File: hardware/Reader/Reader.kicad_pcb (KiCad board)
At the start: 4 copper layers, 136 parts, among them CN1 AHDF15A-KG-TAXB

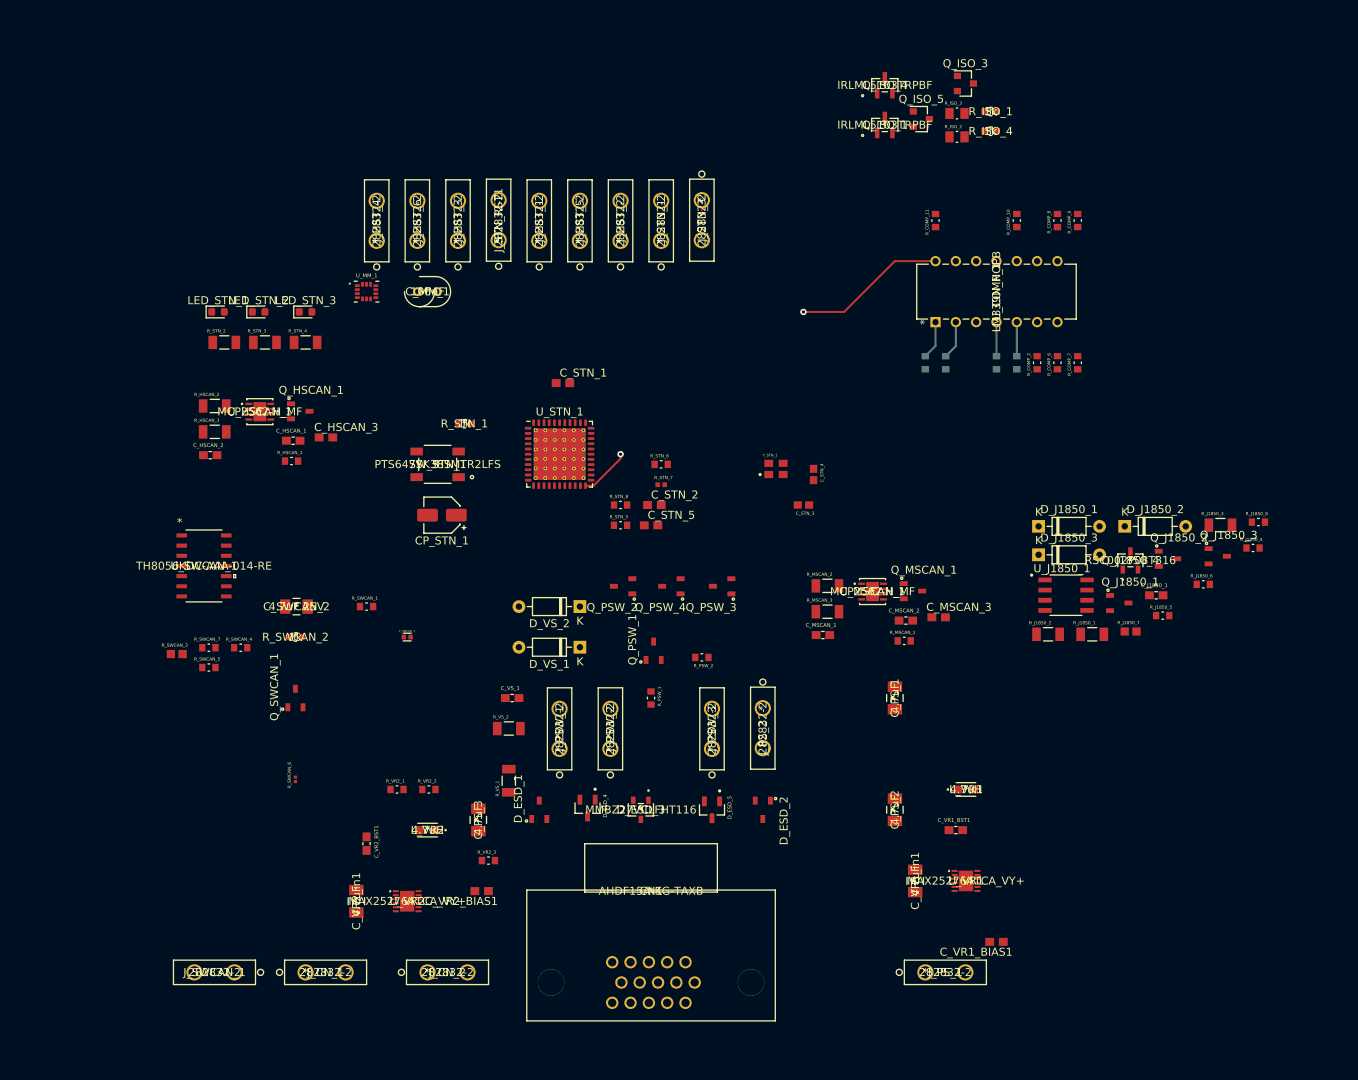
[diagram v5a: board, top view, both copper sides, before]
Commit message: Fixed wiring issue on ESD Protection
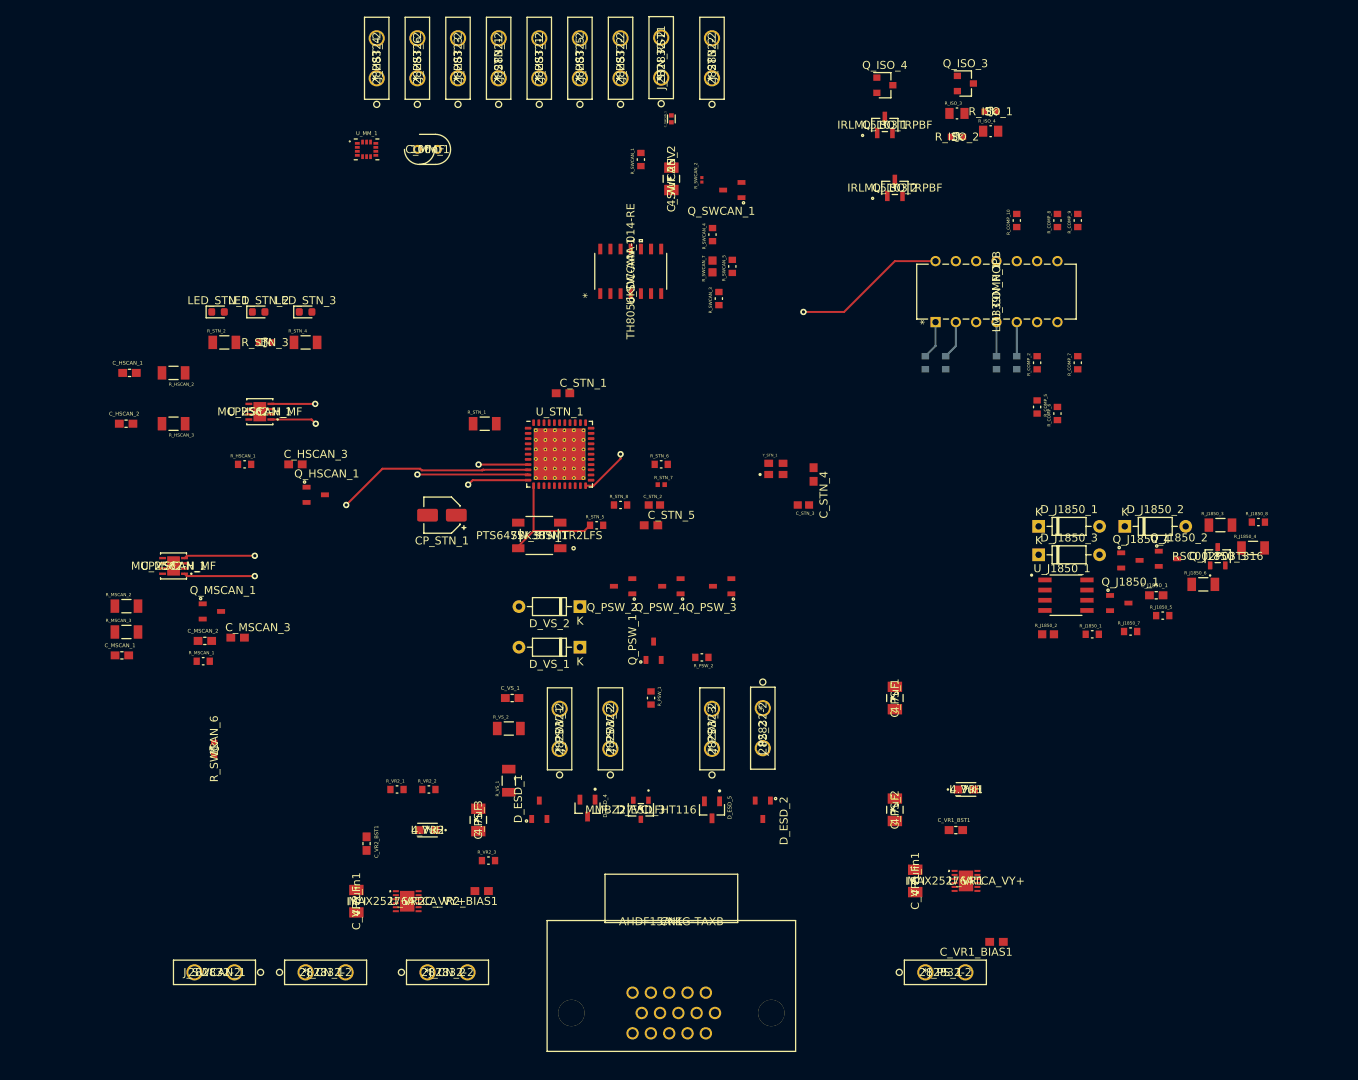
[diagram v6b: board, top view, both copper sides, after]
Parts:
- removed J_STN_3: 282832-2, footprints:282832-2
- removed Q_ISO_5: MMBT3904WT1G, Package_TO_SOT_SMD:SOT-23
- removed R_COMP5, R_COMP_11: 10k, footprints:RESC1608X55N
- added J_STN_2: 282832-2, footprints:282832-2, F.Cu at (147.3, 35.6)
- added Q_ISO_2: IRLML5103TRPBF, footprints:IRLML5103TRPBF, F.Cu at (170.2, 49.3)
- added R_COMP1: 10k, footprints:RESC1608X55N, B.Cu at (174.0, 71.1)
- added R_COMP_5: 10k, footprints:RESC1608X55N, F.Cu at (188.0, 76.7)
- C_STN_2: value 1uF -> 30pF; footprint footprints:0603 -> footprints:CAPC1608X90N
- C_STN_4: value 30pF -> 1uF; footprint footprints:CAPC1608X90N -> footprints:0603
- D_ESD_4, D_ESD_5: footprint footprints:SOT95P237X111-3N -> SOT95P237X111-3N
- Q_ISO_4: value IRLML5103TRPBF -> MMBT3904WT1G; footprint footprints:IRLML5103TRPBF -> Package_TO_SOT_SMD:SOT-23
- Q_J1850_3: value NX7002AK,215 -> RSC002P03T316; footprint footprints:SOT95P230X110-3N -> footprints:RSC002P03T316
- Q_J1850_4: value RSC002P03T316 -> NX7002AK,215; footprint footprints:RSC002P03T316 -> footprints:SOT95P230X110-3N
- R_COMP_7: value 10k -> 2.7k
- R_COMP_8: value 2.7k -> 10k
- R_ISO_2: value 510k/0.5W -> 1k; footprint footprints:RESC2012X70N -> footprints:RC1608F102CS
- R_ISO_4: value 1k -> 510k/0.5W; footprint footprints:RC1608F102CS -> footprints:RESC2012X70N
- R_J1850_1: value 374 -> 10k; footprint footprints:RESC3216X70N -> footprints:RESC1608X55N
- R_J1850_2: value 866 -> 1.5k; footprint footprints:RESC3216X70N -> footprints:RESC1607X60N
- R_J1850_3: value 240 -> 866
- R_J1850_4: value 10k -> 374; footprint footprints:RESC1608X55N -> footprints:RESC3216X70N
- R_J1850_6: value 10k -> 240; footprint footprints:RESC1608X55N -> footprints:RESC3216X70N
- R_J1850_7: value 1.5k -> 10k; footprint footprints:RESC1607X60N -> footprints:RESC1608X55N
- R_STN_1: value 1k -> 330; footprint footprints:RC1608F102CS -> footprints:RESC3216X70N
- R_STN_3: value 330 -> 1k; footprint footprints:RESC3216X70N -> footprints:RC1608F102CS
- R_SWCAN_1: value 6.49k 0.12W -> 10k
- R_SWCAN_2: value 1k -> 130; footprint footprints:RC1608F102CS -> footprints:RESC0603X26N
- R_SWCAN_3: value 1.5k -> 6.49k 0.12W; footprint footprints:RESC1607X60N -> footprints:RESC1608X55N
- R_SWCAN_6: value 130 -> 1k; footprint footprints:RESC0603X26N -> footprints:RC1608F102CS
- R_SWCAN_7: value 10k -> 1.5k; footprint footprints:RESC1608X55N -> footprints:RESC1607X60N
- moved C_MSCAN_2 87.7 mm to (83.9, 105.9)
- moved C_MSCAN_3 87.7 mm to (88.0, 105.5)
- moved R_MSCAN_2 87.7 mm to (74.1, 101.5)
- moved R_MSCAN_3 87.7 mm to (74.1, 104.8)
- moved C_MSCAN_1 87.7 mm to (73.6, 107.7)
- moved Q_MSCAN_1 87.7 mm to (84.8, 102.2)
- moved R_MSCAN_1 87.7 mm to (83.7, 108.4)
- moved U_MSCAN_1 87.4 mm to (80.0, 96.5), turned to 180 degrees
- moved Q_SWCAN_1 83.8 mm to (149.9, 49.5), turned to 180 degrees
- moved R_SWCAN_5 82.4 mm to (149.9, 59.1), turned to 90 degrees
- moved R_SWCAN_3 81.0 mm to (148.2, 63.1), turned to 90 degrees
- moved R_SWCAN_7 79.0 mm to (147.4, 59.1), turned to 90 degrees
- moved R_SWCAN_4 78.4 mm to (147.4, 55.1), turned to 90 degrees
- moved R_SWCAN_2 76.5 mm to (146.1, 48.3), turned to 90 degrees
- moved C_SWCAN_1 72.7 mm to (142.2, 40.6), turned to 90 degrees
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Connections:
- CN1 pad 11: Pin14_ISO15765-4_CAN_BUS_Low -> Pin6_ISO15765_CAN_BUS_High
- CN1 pad 12: Pin14_ISO15765-4_CAN_BUS_Low -> Pin14_ISO15765_CAN_BUS_Low
- CN1 pad 6: Pin15_ISO9141_L-Line -> Pin7_ISO9141_K-Line
- C_STN_2 pad 1: +3V3 -> Pin4_GnD_Chassis
- C_STN_2 pad 2: Pin4_GnD_Chassis -> Net-(C_STN_2-Pad2)
- C_STN_3 pad 1: Pin4_GnD_Chassis -> Net-(C_STN_3-Pad1)
- C_STN_3 pad 2: Net-(C_STN_3-Pad2) -> Pin4_GnD_Chassis
- C_STN_5 pad 1: Net-(C_STN_5-Pad1) -> +3V3
- D_ESD_1 pad 1: Pin14_ISO15765-4_CAN_BUS_Low -> Pin6_ISO15765_CAN_BUS_High
- D_ESD_1 pad 2: Pin14_ISO15765-4_CAN_BUS_Low -> Pin14_ISO15765_CAN_BUS_Low
- D_ESD_4 pad 1: Pin15_ISO9141_L-Line -> Pin7_ISO9141_K-Line
- D_J1850_1 pad 1: Net-(D_J1850_1-Pad1) -> Pin2_SAE_J1850_BUS+
- D_J1850_1 pad 2: +5V_SW -> Net-(D_J1850_1-Pad2)
- D_J1850_2 pad 1: Pin2_SAE_J1850_BUS+ -> Pin4_GnD_Chassis
- D_J1850_3 pad 1: Pin4_GnD_Chassis -> Net-(D_J1850_3-Pad1)
- D_J1850_3 pad 2: Net-(D_J1850_3-Pad2) -> +5V_SW
- J_CN_1 pad 1: Pin14_ISO15765-4_CAN_BUS_Low -> Pin6_ISO15765_CAN_BUS_High
- J_CN_1 pad 2: Pin14_ISO15765-4_CAN_BUS_Low -> Pin14_ISO15765_CAN_BUS_Low
- J_CN_2 pad 1: Pin15_ISO9141_L-Line -> Pin7_ISO9141_K-Line
- J_HST_2 pad 1: /Host/HOST_RX -> +5V
- J_HST_2 pad 2: /Host/HOST_TX -> Pin4_GnD_Chassis
- J_HST_3 pad 1: /Host/I2C_SCL -> /Host/HOST_RX
- J_HST_3 pad 2: /Host/I2C_SDA -> /Host/HOST_TX
- J_HST_4 pad 1: /Host/MEMS_INT -> /Host/I2C_SCL
- J_HST_4 pad 2: /Host/MEMS_CS -> /Host/I2C_SDA
- J_HST_5 pad 1: +5V -> Pin4_GnD_Chassis
- J_HST_5 pad 2: Pin4_GnD_Chassis -> /Host/MEMS_CS
- J_HST_6 pad 1: Pin4_GnD_Chassis -> /Host/MEMS_INT
- Q_ISO_3 pad 3: Pin15_ISO9141_L-Line -> Pin7_ISO9141_K-Line
- Q_ISO_4 pad 1: /OBDII Interpreter/PWR_CTRL -> Net-(Q_ISO_4-Pad1)
- Q_ISO_4 pad 2: Net-(Q_ISO_4-Pad2) -> Pin4_GnD_Chassis
- Q_ISO_4 pad 3: +12V -> Pin15_ISO9141_L-Line
- Q_J1850_2 pad 1: /OBDII Interpreter/OBDII Chip/J1850_BUS-_TX -> /OBDII Interpreter/OBDII Chip/J1850_BUS+_TX
- Q_J1850_2 pad 3: Pin10_SAE_J1850_BUS- -> Net-(Q_J1850_2-Pad3)
- Q_J1850_3 pad 1: /OBDII Interpreter/OBDII Chip/J1850_BUS+_TX -> Net-(Q_J1850_2-Pad3)
- Q_J1850_3 pad 2: Pin4_GnD_Chassis -> +V_J1850
- Q_J1850_3 pad 3: Net-(Q_J1850_3-Pad3) -> Net-(D_J1850_1-Pad2)
- Q_J1850_4 pad 1: Net-(Q_J1850_3-Pad3) -> /OBDII Interpreter/OBDII Chip/J1850_BUS-_TX
- Q_J1850_4 pad 2: +V_J1850 -> Pin4_GnD_Chassis
- Q_J1850_4 pad 3: Net-(D_J1850_2-Pad2) -> Pin10_SAE_J1850_BUS-
- R_COMP_10 pad 1: Net-(R_COMP_10-Pad1) -> +3V3
- R_COMP_10 pad 2: Pin2_SAE_J1850_BUS+ -> /OBDII Interpreter/Comparator Transceiver/VPW_RX
- R_COMP_2 pad 1: Pin15_ISO9141_L-Line -> Pin7_ISO9141_K-Line
- R_COMP_6 pad 1: +12V_SW -> Net-(R_COMP_5-Pad2)
- R_COMP_6 pad 2: Net-(R_COMP_6-Pad2) -> Pin4_GnD_Chassis
- R_COMP_7 pad 1: Net-(R_COMP_6-Pad2) -> +5V_SW
- R_COMP_7 pad 2: Pin4_GnD_Chassis -> Net-(R_COMP_7-Pad2)
- R_COMP_8 pad 1: +5V_SW -> Net-(R_COMP_7-Pad2)
- R_COMP_8 pad 2: Net-(R_COMP_8-Pad2) -> Pin4_GnD_Chassis
- R_COMP_9 pad 1: Net-(R_COMP_8-Pad2) -> Net-(R_COMP_9-Pad1)
- R_COMP_9 pad 2: Pin4_GnD_Chassis -> Pin2_SAE_J1850_BUS+
- R_HSCAN_2 pad 1: Pin14_ISO15765-4_CAN_BUS_Low -> Pin14_ISO15765_CAN_BUS_Low
- R_HSCAN_3 pad 1: Pin14_ISO15765-4_CAN_BUS_Low -> Pin6_ISO15765_CAN_BUS_High
- R_ISO_2 pad 1: Pin15_ISO9141_L-Line -> Net-(Q_ISO_4-Pad1)
- R_ISO_2 pad 2: Net-(Q_ISO_1-Pad2) -> /OBDII Interpreter/ISO 9141/ISO 14230 Transceiver/~ISO_L_TX~
- R_ISO_3 pad 1: Pin15_ISO9141_L-Line -> Pin7_ISO9141_K-Line
- R_ISO_3 pad 2: Net-(Q_ISO_4-Pad2) -> Net-(Q_ISO_1-Pad2)
- R_ISO_4 pad 1: Net-(Q_ISO_5-Pad1) -> Pin15_ISO9141_L-Line
- R_ISO_4 pad 2: /OBDII Interpreter/ISO 9141/ISO 14230 Transceiver/~ISO_L_TX~ -> Net-(Q_ISO_2-Pad2)
- R_J1850_1 pad 1: Net-(Q_J1850_1-Pad3) -> /OBDII Interpreter/OBDII Chip/J1850_BUS+_TX
- R_J1850_2 pad 1: Net-(Q_J1850_1-Pad3) -> +V_J1850
- R_J1850_2 pad 2: Net-(R_J1850_2-Pad2) -> Net-(Q_J1850_2-Pad3)
- R_J1850_3 pad 1: +V_J1850 -> Net-(Q_J1850_1-Pad3)
- R_J1850_3 pad 2: Net-(R_J1850_2-Pad2) -> Net-(R_J1850_3-Pad2)
- R_J1850_4 pad 1: /OBDII Interpreter/OBDII Chip/J1850_BUS-_TX -> Net-(Q_J1850_1-Pad3)
- R_J1850_5 pad 1: Net-(D_J1850_1-Pad1) -> Pin2_SAE_J1850_BUS+
- R_J1850_5 pad 2: Pin10_SAE_J1850_BUS- -> Net-(D_J1850_2-Pad2)
- R_J1850_6 pad 1: /OBDII Interpreter/OBDII Chip/J1850_BUS+_TX -> +V_J1850
- R_J1850_6 pad 2: Pin4_GnD_Chassis -> Net-(R_J1850_3-Pad2)
- R_J1850_7 pad 1: +V_J1850 -> /OBDII Interpreter/OBDII Chip/J1850_BUS-_TX
- R_J1850_7 pad 2: Net-(Q_J1850_3-Pad3) -> Pin4_GnD_Chassis
- R_J1850_8 pad 1: Pin2_SAE_J1850_BUS+ -> Net-(D_J1850_3-Pad1)
- R_J1850_8 pad 2: Net-(D_J1850_3-Pad2) -> Pin10_SAE_J1850_BUS-
- R_STN_1 pad 1: +3V3 -> Net-(LED_STN_1-Pad1)
- R_STN_1 pad 2: /Host/HOST_TX -> /OBDII Interpreter/OBDII Chip/STATUS_LED
- R_STN_2 pad 1: Net-(LED_STN_1-Pad1) -> Net-(LED_STN_2-Pad1)
- R_STN_2 pad 2: /OBDII Interpreter/OBDII Chip/STATUS_LED -> /OBDII Interpreter/~RESET_OBD_HW~
- R_STN_3 pad 1: Net-(LED_STN_2-Pad1) -> +3V3
- R_STN_3 pad 2: /OBDII Interpreter/~RESET_OBD_HW~ -> /Host/HOST_TX
- R_SWCAN_1 pad 1: Pin1_SW_CAN -> /OBDII Interpreter/OBDII Chip/SW_CAN_LOAD
- R_SWCAN_1 pad 2: Net-(R_SWCAN_1-Pad2) -> Pin4_GnD_Chassis
- R_SWCAN_2 pad 1: /OBDII Interpreter/OBDII Chip/SW_CAN_RX -> Net-(J_SWCAN_1-Pad2)
- R_SWCAN_2 pad 2: +3V3 -> Net-(Q_SWCAN_1-Pad3)
- R_SWCAN_3 pad 1: /OBDII Interpreter/OBDII Chip/SW_CAN_TX -> Pin1_SW_CAN
- R_SWCAN_3 pad 2: +5V -> Net-(R_SWCAN_3-Pad2)
- R_SWCAN_6 pad 1: Net-(J_SWCAN_1-Pad2) -> /OBDII Interpreter/OBDII Chip/SW_CAN_RX
- R_SWCAN_6 pad 2: Net-(Q_SWCAN_1-Pad3) -> +3V3
- R_SWCAN_7 pad 1: /OBDII Interpreter/OBDII Chip/SW_CAN_LOAD -> /OBDII Interpreter/OBDII Chip/SW_CAN_TX
- R_SWCAN_7 pad 2: Pin4_GnD_Chassis -> +5V
- U_COMP_1 pad 7: Net-(R_COMP_6-Pad2) -> Net-(R_COMP_5-Pad2)
- U_COMP_1 pad 8: Net-(R_COMP_8-Pad2) -> Net-(R_COMP_7-Pad2)
- U_COMP_1 pad 9: Net-(R_COMP_10-Pad1) -> Net-(R_COMP_9-Pad1)
- U_HSCAN_1 pad 6: Pin14_ISO15765-4_CAN_BUS_Low -> Pin14_ISO15765_CAN_BUS_Low
- U_HSCAN_1 pad 7: Pin14_ISO15765-4_CAN_BUS_Low -> Pin6_ISO15765_CAN_BUS_High
- U_J1850_1 pad 4: Net-(R_J1850_2-Pad2) -> Net-(R_J1850_3-Pad2)
- U_STN_1 pad 29: Net-(C_STN_5-Pad1) -> Net-(C_STN_4-Pad1)
- U_STN_1 pad 30: Net-(C_STN_4-Pad1) -> Net-(C_STN_3-Pad1)
- U_STN_1 pad 31: Net-(C_STN_3-Pad2) -> Net-(C_STN_2-Pad2)
- U_SWCAN_1 pad 11: Net-(R_SWCAN_1-Pad2) -> Net-(R_SWCAN_3-Pad2)
- Y_STN_1 pad 1: Net-(C_STN_3-Pad2) -> Net-(C_STN_2-Pad2)
- Y_STN_1 pad 3: Net-(C_STN_4-Pad1) -> Net-(C_STN_3-Pad1)
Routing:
- net /OBDII Interpreter/High Speed CAN Transceiver/HS_CAN_RX: track 0.00 -> 89.3 mm, vias 0 -> 2
- net /OBDII Interpreter/High Speed CAN Transceiver/HS_CAN_TX: track 0.00 -> 88.8 mm, vias 0 -> 2
- net /OBDII Interpreter/Medium Speed CAN Transceiver/MS_CAN_TX: track 0.00 -> 49.0 mm, vias 0 -> 2
- net /OBDII Interpreter/Medium Speed CAN Transceiver/MS_CAN_RX: track 0.00 -> 47.0 mm, vias 0 -> 2
- net /OBDII Interpreter/~RESET_OBD_HW~: track 0.11 -> 16.1 mm
- net /OBDII Interpreter/~PWR_CTRL~: track 1.27 -> 0.00 mm

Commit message: Fixed minor bugs in schematic. Completed PCB layout v0.0.1 and exported Gerber files
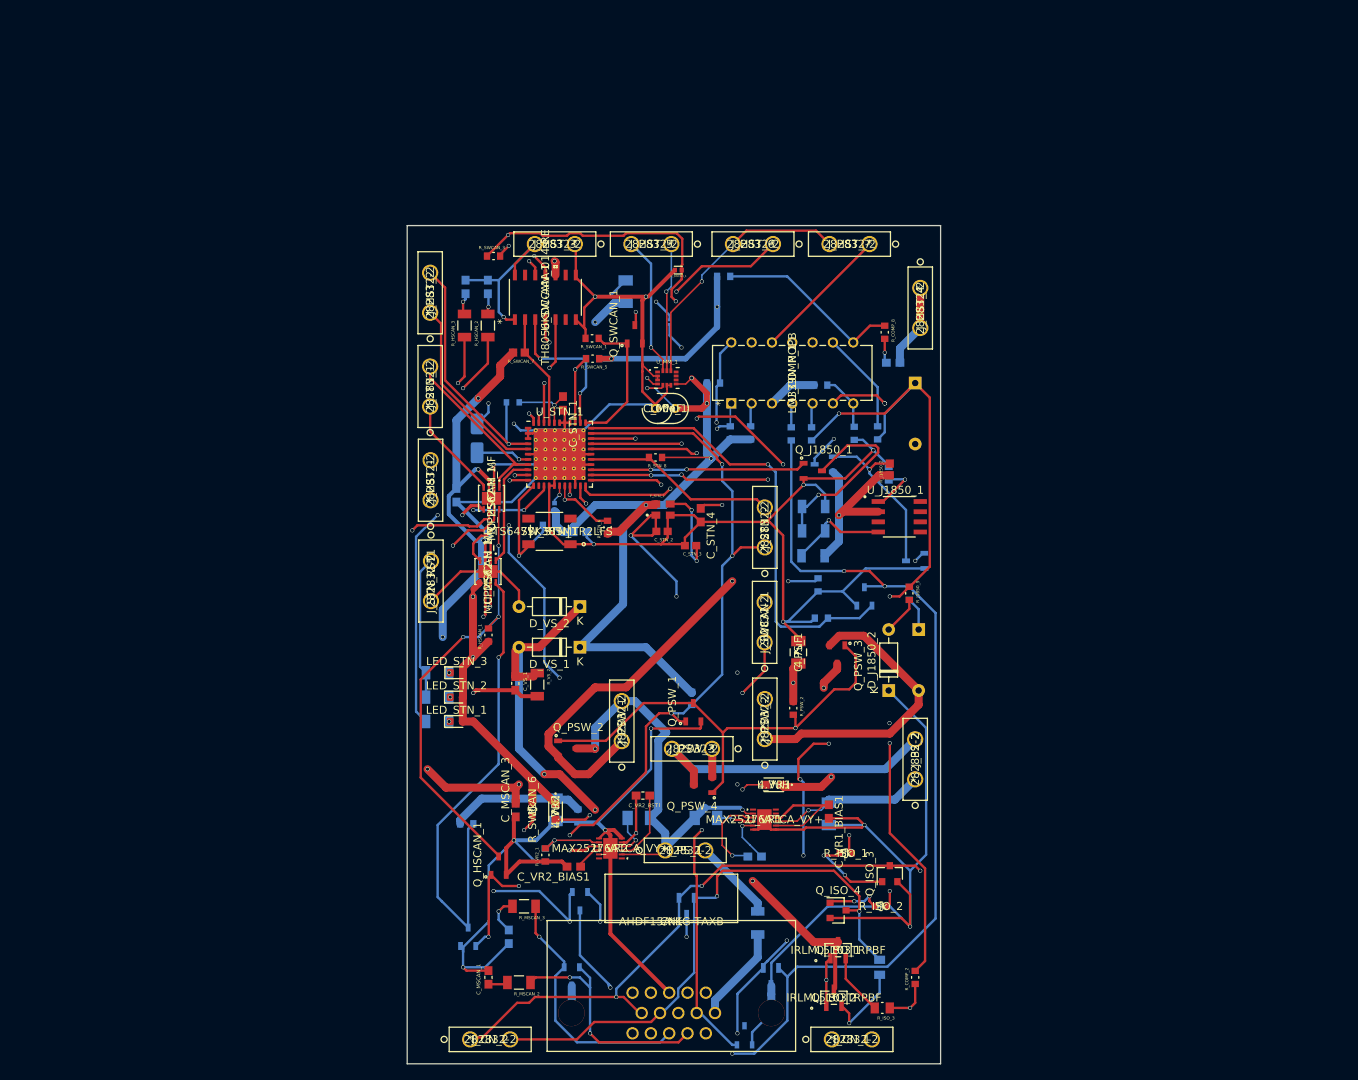
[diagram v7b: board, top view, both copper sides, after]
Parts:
- added C_HST_1: 1uF, footprints:0603, B.Cu at (170.0, 71.1)
- added J_HST_3: 282832-2, footprints:282832-2, F.Cu at (130.2, 56.3)
- CP_STN_1, C_HSCAN_1, C_HSCAN_2, C_HSCAN_3, C_J1850_1, C_MSCAN_2, C_PS_2, C_PS_3, C_STN_5, C_SWCAN_2, C_VR1_BST1, C_VR1_in1, C_VR2_in1, D_ESD_1, D_ESD_2, D_ESD_3, D_ESD_4, D_ESD_5, D_J1850_1, D_J1850_3, Q_J1850_2, Q_J1850_3, Q_J1850_4, Q_MSCAN_1, R_COMP_10, R_COMP_5, R_COMP_6, R_COMP_7, R_COMP_9, R_ISO_4, R_J1850_1, R_J1850_3, R_J1850_4, R_J1850_6, R_J1850_7, R_J1850_8, R_MSCAN_1, R_PSW_1, R_STN_1, R_STN_2, R_STN_3, R_STN_4, R_STN_5, R_STN_7, R_SWCAN_2, R_SWCAN_4, R_VR2_2, R_VR2_3, R_VS_1: moved to B.Cu
- moved R_ISO_3 112.2 mm to (168.6, 151.8), turned to 180 degrees
- moved R_ISO_4 105.4 mm to (168.3, 146.7), turned to 270 degrees
- moved Q_ISO_1 103.3 mm to (163.1, 144.5)
- moved Q_ISO_4 103.3 mm to (163.1, 139.6)
- moved Q_ISO_2 101.5 mm to (162.6, 150.5)
- moved Q_ISO_3 99.2 mm to (169.5, 135.0), turned to 90 degrees
- moved R_ISO_2 96.6 mm to (168.4, 139.1)
- moved R_ISO_1 94.5 mm to (164.0, 132.4)
- moved R_COMP_2 78.3 mm to (172.7, 148.0)
- moved J_SWCAN_1 78.1 mm to (153.9, 106.1), turned to 90 degrees
- moved R_MSCAN_2 68.0 mm to (123.2, 148.6), turned to 180 degrees
- moved J_STN_RST1 66.9 mm to (112.2, 95.9), turned to 270 degrees
- moved J_CN_1 66.3 mm to (162.3, 155.7)
- moved C_MSCAN_1 61.0 mm to (119.4, 148.0), turned to 90 degrees
- moved R_MSCAN_3 60.4 mm to (123.8, 139.1), turned to 180 degrees
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- renumbered J_HST_3 to J_HST_2, J_HST_2 to J_HST_4, J_HST_4 to J_HST_5, J_HST_5 to J_HST_7
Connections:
- C_MM_1 pad 1: +3.3V_SW -> +3V3
- J_HST_4 pad 2: Pin4_GnD_Chassis -> +5V
- U_MM_1 pad 5: +3.3V_SW -> +3V3
- U_MM_1 pad 8: +3.3V_SW -> +3V3
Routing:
- net Pin4_GnD_Chassis: track 0.00 -> 722.4 mm, vias 0 -> 21
- net +3V3: track 0.00 -> 309.8 mm, vias 0 -> 11
- net +5V: track 0.00 -> 280.5 mm, vias 0 -> 9
- net +12V: track 0.00 -> 181.5 mm, vias 0 -> 7
- net Pin14_ISO15765_CAN_BUS_Low: track 0.00 -> 153.2 mm, vias 0 -> 3
- net Pin1_SW_CAN: track 0.00 -> 146.9 mm, vias 0 -> 6
- net Pin6_ISO15765_CAN_BUS_High: track 0.00 -> 139.6 mm, vias 0 -> 4
- net Pin2_SAE_J1850_BUS+: track 0.00 -> 135.0 mm, vias 0 -> 7
- net +5V_SW: track 0.00 -> 132.1 mm, vias 0 -> 2
- net Pin10_SAE_J1850_BUS-: track 0.00 -> 125.1 mm, vias 0 -> 3
- net /OBDII Interpreter/~PWR_CTRL~: track 0.00 -> 105.9 mm, vias 0 -> 6
- net /OBDII Interpreter/PWR_CTRL: track 0.00 -> 97.6 mm, vias 0 -> 2
- net Pin7_ISO9141_K-Line: track 0.00 -> 96.4 mm, vias 0 -> 4
- net /OBDII Interpreter/ISO 9141/ISO 14230 Transceiver/~ISO_L_TX~: track 0.00 -> 89.9 mm, vias 0 -> 2
- net Pin3_MS_CAN_High: track 0.00 -> 87.8 mm, vias 0 -> 2
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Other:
- board outline added: 66.7 x 104.8 mm
- net class Default: via_dia 0.8 -> 0.5
- net class Power added: clearance 0.2, trace_width 0.7, via_dia 0.5, via_drill 0.4
- rule via_min_drill: 0.305 -> 0.3
- rule via_min_size: 0.4 -> 0.2
- board text added: "CANtech | CANnect Reader v0.0.1"

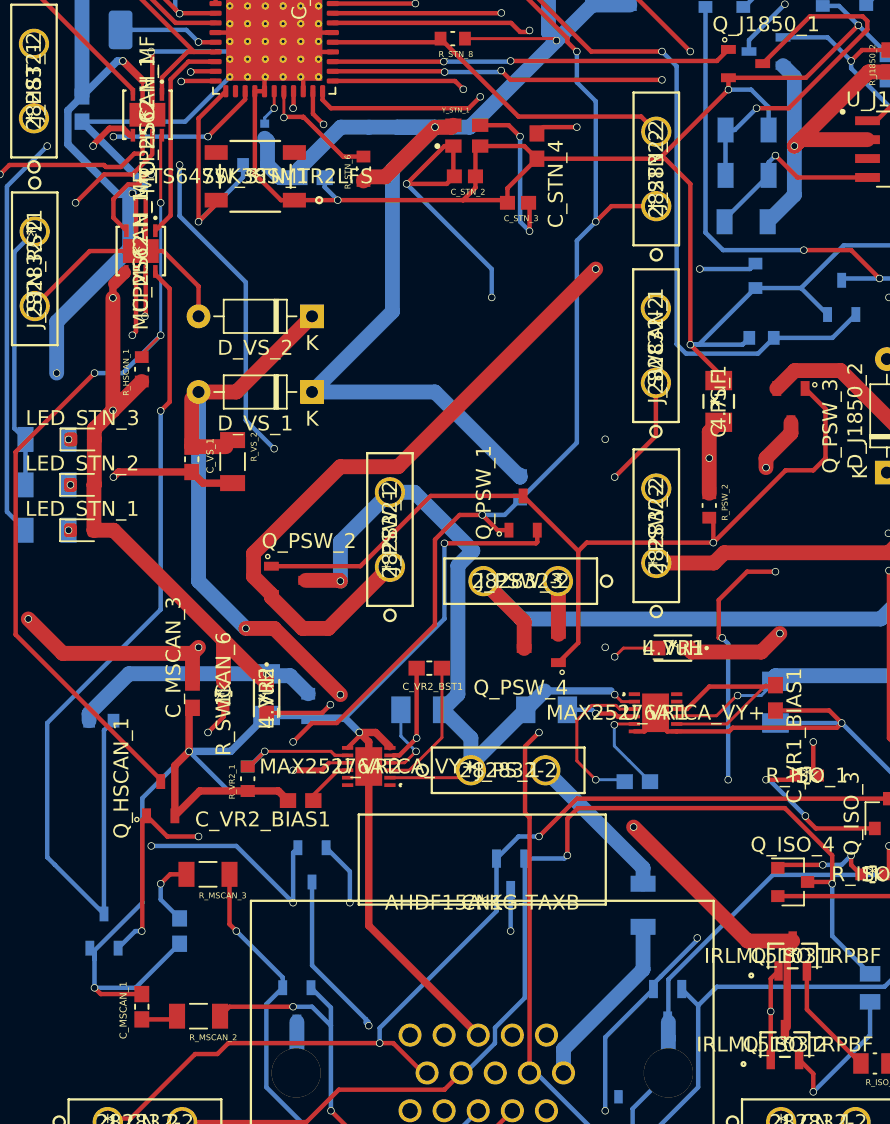
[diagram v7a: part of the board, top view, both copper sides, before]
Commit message: Addressed Design Rules problems
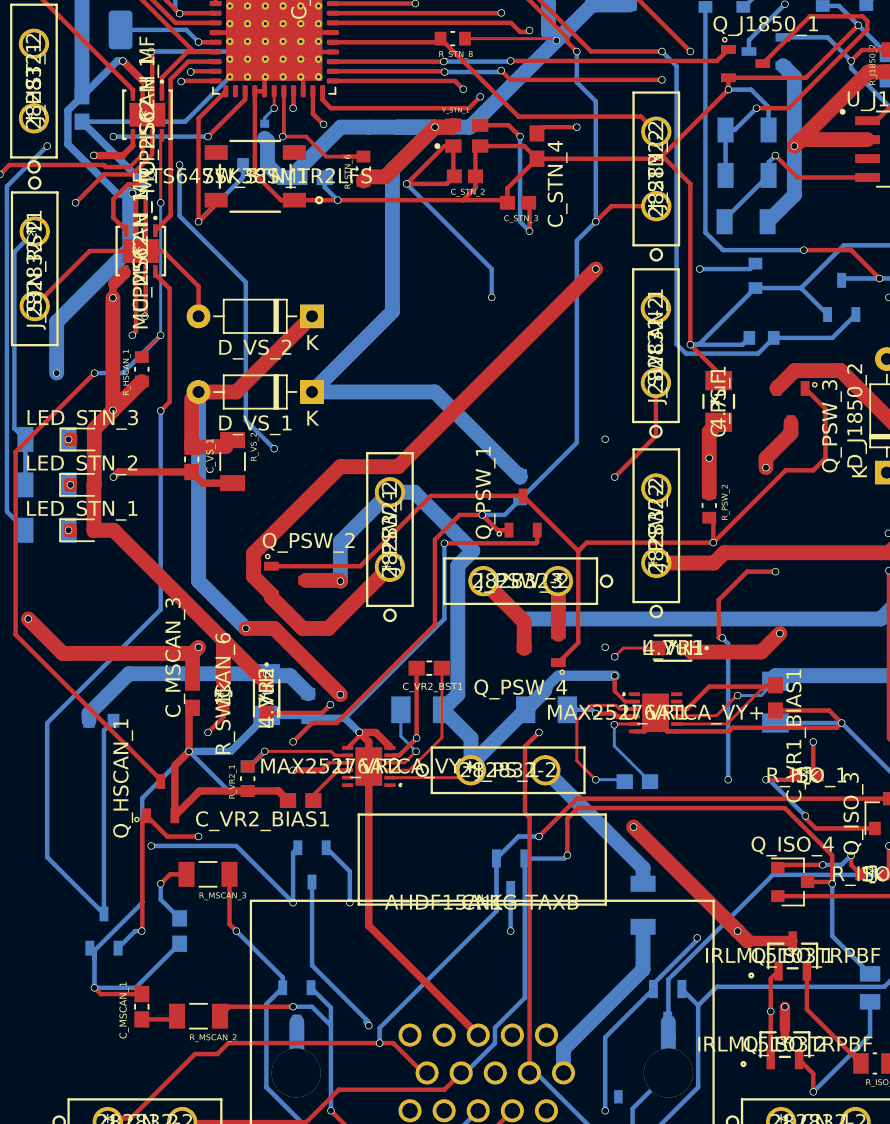
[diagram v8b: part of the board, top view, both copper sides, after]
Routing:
- net +12V: track 181.5 -> 186.8 mm, vias 7 -> 9
- net /OBDII Interpreter/RESET_OBD_SW: track 27.6 -> 28.9 mm
